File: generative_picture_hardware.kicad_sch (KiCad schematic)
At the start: 46 parts, among them J1 e_Paper_HAT, J2 Conn_ARM_JTAG_SWD_10, J3 USB_C_Receptacle_USB2.0, Q1 PMN48XP, Q2 MBT3904DW1, SW1 SW_Push, SW2 SW_Push, U1 AP2112K-3.3, U2 ESP32-WROOM-32, U3 MCP73831-2ACI-OT, U4 FT231XS, U5 SRV05-4HTG-D

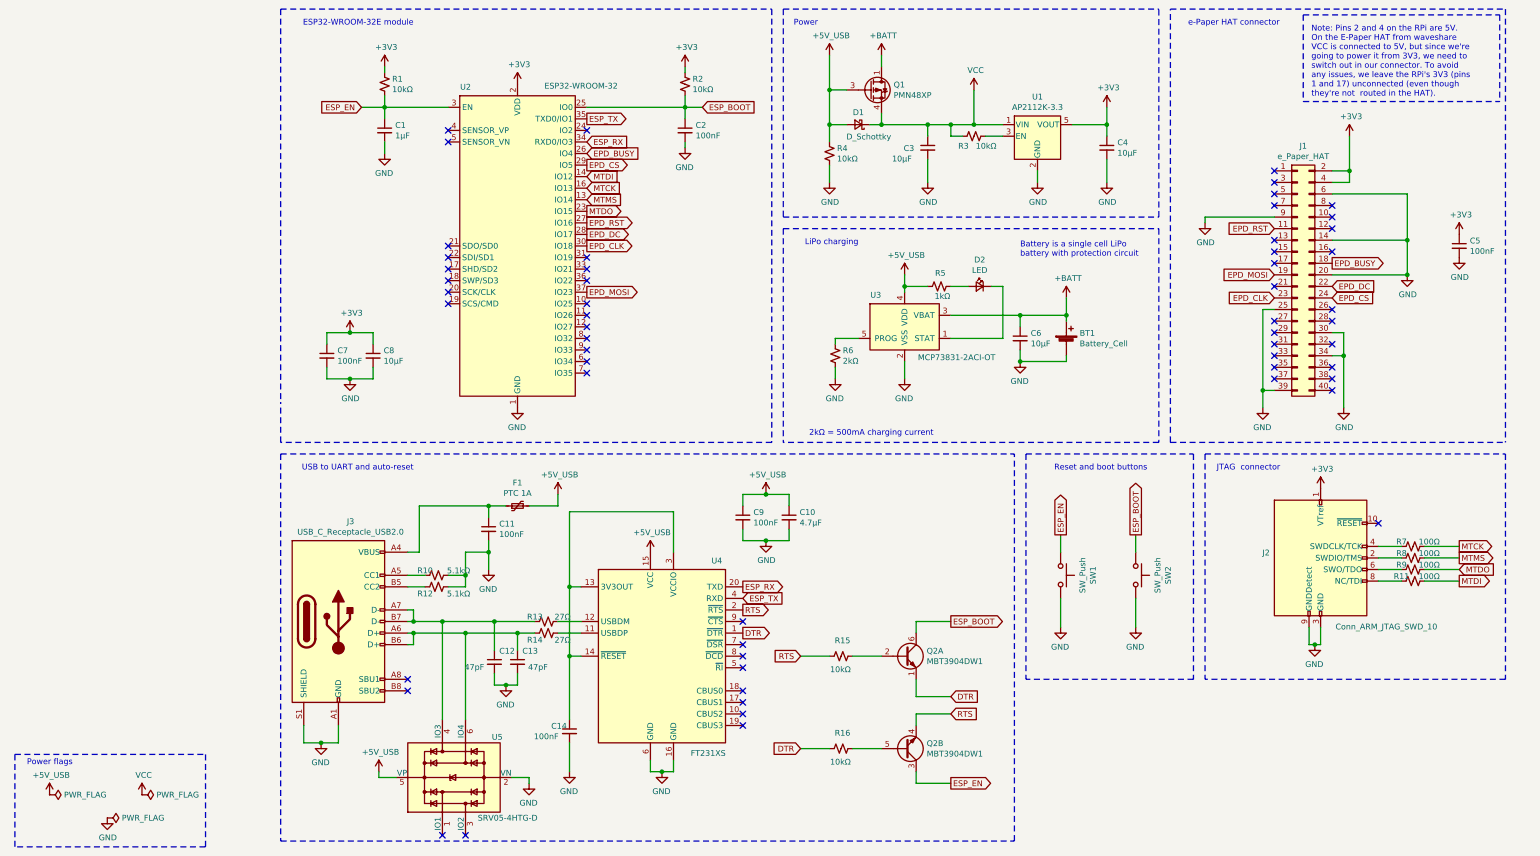
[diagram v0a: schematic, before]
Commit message: Adds battery protection circuit with AP9101
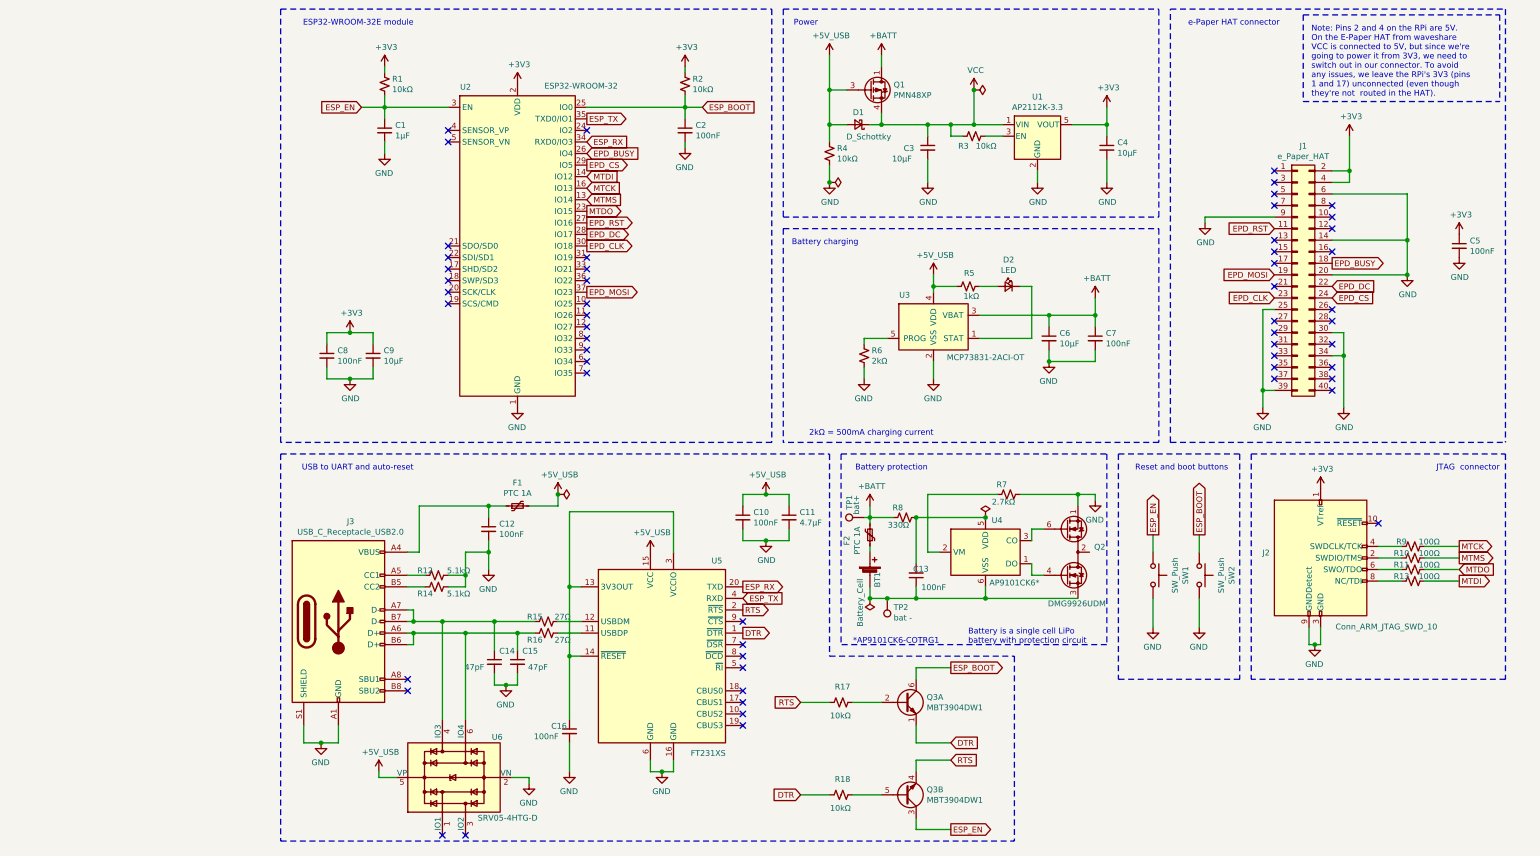
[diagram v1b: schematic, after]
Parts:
- added C13, C7: 100nF, symbol Device:C_Small
- added F2: PTC 1A, symbol Device:Polyfuse_Small
- added Q2: DMG9926UDM, Package_TO_SOT_SMD:SOT-23-6, symbol Transistor_FET:DMG9926UDM
- added R7: 2.7kΩ, symbol Device:R_Small_US
- added R8: 330Ω, symbol Device:R_Small_US
- added TP1: bat+, symbol Connector:TestPoint
- added TP2: bat -, symbol Connector:TestPoint
- added U4: AP9101CK6*, Package_TO_SOT_SMD:SOT-23-6, symbol Battery_Management:AP9101CK6
- renumbered C9 to C10, C10 to C11, C11 to C12, C12 to C14, C13 to C15, C14 to C16, C7 to C8, C8 to C9, Q2 to Q3, R8 to R10, R9 to R11, R10 to R12, R11 to R13, R12 to R14, R13 to R15, R14 to R16, R15 to R17, R16 to R18, R7 to R9, U4 to U5, U5 to U6
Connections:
- net +BATT: now also C7.1, F2.2, R8.2, TP1.1; no longer BT1.1 (+)
- net GND: now also C7.2, Q2.1 (D1), R7.1; no longer BT1.2 (-)
- new net: BT1.2 (-), C13.1, Q2.3 (S2), TP2.1, U4.6 (VSS)
- new net: BT1.1 (+), F2.1
- new net: C13.2, R8.1, U4.5 (VDD)
- new net: Q2.2 (S1/D2), Q2.5 (S1/D2)
- new net: Q2.4 (G2), U4.1 (DO)
- new net: Q2.6 (G1), U4.3 (CO)
- new net: R7.2, U4.2 (VM)
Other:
- note added: "*AP9101CK6-COTRG1"
- note added: "Battery charging"
- note added: "Battery protection"
- note removed: "LiPo charging"
- note removed: "Power flags"
- moved on the sheet: C6, D2, Q3A, Q3B, R17, R18, R5, R6, SW1, SW2, U3

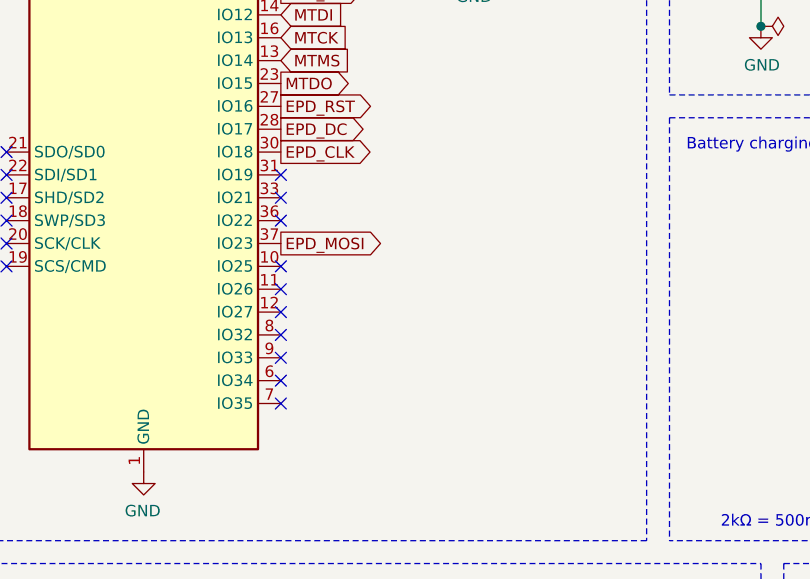
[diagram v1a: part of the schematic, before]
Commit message: Adds test points to some of the remaining GPIO pins of the ESP32
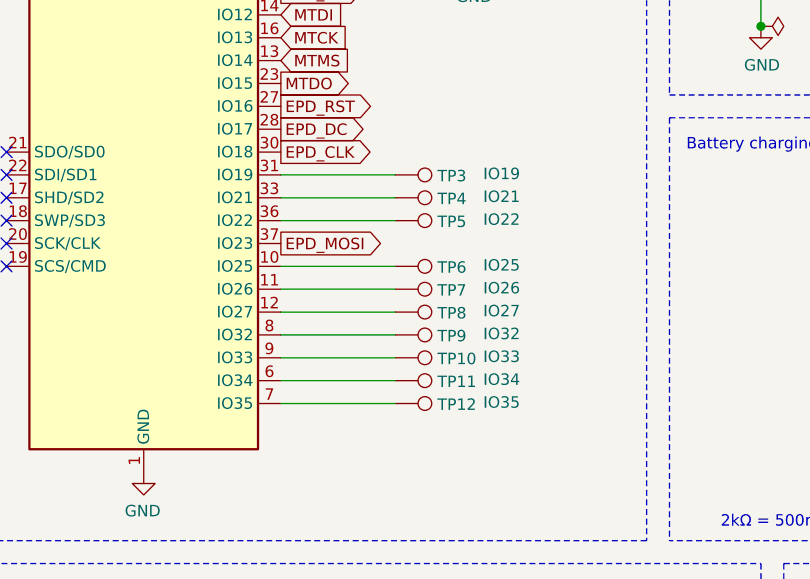
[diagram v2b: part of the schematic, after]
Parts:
- added TP10: IO33, symbol Connector:TestPoint
- added TP11: IO34, symbol Connector:TestPoint
- added TP12: IO35, symbol Connector:TestPoint
- added TP3: IO19, symbol Connector:TestPoint
- added TP4: IO21, symbol Connector:TestPoint
- added TP5: IO22, symbol Connector:TestPoint
- added TP6: IO25, symbol Connector:TestPoint
- added TP7: IO26, symbol Connector:TestPoint
- added TP8: IO27, symbol Connector:TestPoint
- added TP9: IO32, symbol Connector:TestPoint
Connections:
- net at U2.10 (IO25): now also TP6.1
- net at U2.11 (IO26): now also TP7.1
- net at U2.12 (IO27): now also TP8.1
- net at U2.31 (IO19): now also TP3.1
- net at U2.33 (IO21): now also TP4.1
- net at U2.36 (IO22): now also TP5.1
- net at U2.6 (IO34): now also TP11.1
- net at U2.7 (IO35): now also TP12.1
- net at U2.8 (IO32): now also TP9.1
- net at U2.9 (IO33): now also TP10.1
- no-connect marks 56 -> 46
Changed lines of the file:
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@@
   (no_connect (at 54.61 195.58))
   (no_connect (at 81.28 40.64))
-  (no_connect (at 81.28 68.58))
-  (no_connect (at 81.28 71.12))
-  (no_connect (at 81.28 73.66))
-  (no_connect (at 81.28 78.74))
-  (no_connect (at 81.28 81.28))
-  (no_connect (at 81.28 83.82))
-  (no_connect (at 81.28 86.36))
-  (no_connect (at 81.28 88.9))
-  (no_connect (at 81.28 91.44))
-  (no_connect (at 81.28 93.98))
   (no_connect (at 115.57 148.59))
   (no_connect (at 115.57 153.67))
@@
     (stroke (width 0) (type solid) (color 0 0 0 0))
   )
+  (wire (pts (xy 81.28 68.58) (xy 93.98 68.58))
+    (stroke (width 0) (type solid) (color 0 0 0 0))
+  )
+  (wire (pts (xy 81.28 71.12) (xy 93.98 71.12))
+    (stroke (width 0) (type solid) (color 0 0 0 0))
+  )
+  (wire (pts (xy 81.28 73.66) (xy 93.98 73.66))
+    (stroke (width 0) (type solid) (color 0 0 0 0))
+  )
+  (wire (pts (xy 81.28 78.74) (xy 93.98 78.74))
+    (stroke (width 0) (type solid) (color 0 0 0 0))
+  )
+  (wire (pts (xy 81.28 81.28) (xy 93.98 81.28))
+    (stroke (width 0) (type solid) (color 0 0 0 0))
+  )
+  (wire (pts (xy 81.28 83.82) (xy 93.98 83.82))
+    (stroke (width 0) (type solid) (color 0 0 0 0))
+  )
+  (wire (pts (xy 81.28 86.36) (xy 93.98 86.36))
+    (stroke (width 0) (type solid) (color 0 0 0 0))
+  )
+  (wire (pts (xy 81.28 88.9) (xy 93.98 88.9))
+    (stroke (width 0) (type solid) (color 0 0 0 0))
+  )
+  (wire (pts (xy 81.28 91.44) (xy 93.98 91.44))
+    (stroke (width 0) (type solid) (color 0 0 0 0))
+  )
+  (wire (pts (xy 81.28 93.98) (xy 93.98 93.98))
+    (stroke (width 0) (type solid) (color 0 0 0 0))
+  )
   (wire (pts (xy 95.25 179.07) (xy 95.25 181.61))
     (stroke (width 0) (type solid) (color 0 0 0 0))
@@
     )
     (property "Datasheet" "~" (id 3) (at 168.91 125.73 0)
+      (effects (font (size 1.27 1.27)) hide)
+    )
+  )
+  (symbol (lib_id "Connector:TestPoint") (at 93.98 68.58 270) (unit 1)
+    (in_bom yes) (on_board yes)
+    (property "Reference" "TP3" (id 0) (at 98.6791 68.7006 90)
+      (effects (font (size 1.27 1.27)) (justify left))
+    )
+    (property "Value" "IO19" (id 1) (at 103.759 68.459 90)
+      (effects (font (size 1.27 1.27)) (justify left))
+    )
+    (property "Footprint" "" (id 2) (at 93.98 73.66 0)
+      (effects (font (size 1.27 1.27)) hide)
+    )
+    (property "Datasheet" "~" (id 3) (at 93.98 73.66 0)
+      (effects (font (size 1.27 1.27)) hide)
+    )
+  )
+  (symbol (lib_id "Connector:TestPoint") (at 93.98 71.12 270) (unit 1)
+    (in_bom yes) (on_board yes)
+    (property "Reference" "TP4" (id 0) (at 98.6791 71.2406 90)
+      (effects (font (size 1.27 1.27)) (justify left))
+    )
+    (property "Value" "IO21" (id 1) (at 103.759 70.999 90)
+      (effects (font (size 1.27 1.27)) (justify left))
+    )
+    (property "Footprint" "" (id 2) (at 93.98 76.2 0)
+      (effects (font (size 1.27 1.27)) hide)
+    )
+    (property "Datasheet" "~" (id 3) (at 93.98 76.2 0)
+      (effects (font (size 1.27 1.27)) hide)
+    )
+  )
+  (symbol (lib_id "Connector:TestPoint") (at 93.98 73.66 270) (unit 1)
+    (in_bom yes) (on_board yes)
+    (property "Reference" "TP5" (id 0) (at 98.6791 73.7806 90)
+      (effects (font (size 1.27 1.27)) (justify left))
+    )
+    (property "Value" "IO22" (id 1) (at 103.759 73.539 90)
+      (effects (font (size 1.27 1.27)) (justify left))
+    )
+    (property "Footprint" "" (id 2) (at 93.98 78.74 0)
+      (effects (font (size 1.27 1.27)) hide)
+    )
+    (property "Datasheet" "~" (id 3) (at 93.98 78.74 0)
+      (effects (font (size 1.27 1.27)) hide)
+    )
+  )
+  (symbol (lib_id "Connector:TestPoint") (at 93.98 78.74 270) (unit 1)
+    (in_bom yes) (on_board yes)
+    (property "Reference" "TP6" (id 0) (at 98.6791 78.8606 90)
+      (effects (font (size 1.27 1.27)) (justify left))
+    )
+    (property "Value" "IO25" (id 1) (at 103.759 78.619 90)
+      (effects (font (size 1.27 1.27)) (justify left))
+    )
+    (property "Footprint" "" (id 2) (at 93.98 83.82 0)
+      (effects (font (size 1.27 1.27)) hide)
+    )
+    (property "Datasheet" "~" (id 3) (at 93.98 83.82 0)
+      (effects (font (size 1.27 1.27)) hide)
+    )
+  )
+  (symbol (lib_id "Connector:TestPoint") (at 93.98 81.28 270) (unit 1)
+    (in_bom yes) (on_board yes)
+    (property "Reference" "TP7" (id 0) (at 98.6791 81.4006 90)
+      (effects (font (size 1.27 1.27)) (justify left))
+    )
+    (property "Value" "IO26" (id 1) (at 103.759 81.159 90)
+      (effects (font (size 1.27 1.27)) (justify left))
+    )
+    (property "Footprint" "" (id 2) (at 93.98 86.36 0)
+      (effects (font (size 1.27 1.27)) hide)
+    )
+    (property "Datasheet" "~" (id 3) (at 93.98 86.36 0)
+      (effects (font (size 1.27 1.27)) hide)
+    )
+  )
+  (symbol (lib_id "Connector:TestPoint") (at 93.98 83.82 270) (unit 1)
+    (in_bom yes) (on_board yes)
+    (property "Reference" "TP8" (id 0) (at 98.6791 83.9406 90)
+      (effects (font (size 1.27 1.27)) (justify left))
+    )
+    (property "Value" "IO27" (id 1) (at 103.759 83.699 90)
+      (effects (font (size 1.27 1.27)) (justify left))
+    )
+    (property "Footprint" "" (id 2) (at 93.98 88.9 0)
+      (effects (font (size 1.27 1.27)) hide)
+    )
+    (property "Datasheet" "~" (id 3) (at 93.98 88.9 0)
+      (effects (font (size 1.27 1.27)) hide)
+    )
+  )
+  (symbol (lib_id "Connector:TestPoint") (at 93.98 86.36 270) (unit 1)
+    (in_bom yes) (on_board yes)
+    (property "Reference" "TP9" (id 0) (at 98.6791 86.4806 90)
+      (effects (font (size 1.27 1.27)) (justify left))
+    )
+    (property "Value" "IO32" (id 1) (at 103.759 86.239 90)
+      (effects (font (size 1.27 1.27)) (justify left))
+    )
+    (property "Footprint" "" (id 2) (at 93.98 91.44 0)
+      (effects (font (size 1.27 1.27)) hide)
+    )
+    (property "Datasheet" "~" (id 3) (at 93.98 91.44 0)
+      (effects (font (size 1.27 1.27)) hide)
+    )
+  )
+  (symbol (lib_id "Connector:TestPoint") (at 93.98 88.9 270) (unit 1)
+    (in_bom yes) (on_board yes)
+    (property "Reference" "TP10" (id 0) (at 98.6791 89.0206 90)
+      (effects (font (size 1.27 1.27)) (justify left))
+    )
+    (property "Value" "IO33" (id 1) (at 103.759 88.779 90)
+      (effects (font (size 1.27 1.27)) (justify left))
+    )
+    (property "Footprint" "" (id 2) (at 93.98 93.98 0)
+      (effects (font (size 1.27 1.27)) hide)
+    )
+    (property "Datasheet" "~" (id 3) (at 93.98 93.98 0)
+      (effects (font (size 1.27 1.27)) hide)
+    )
+  )
+  (symbol (lib_id "Connector:TestPoint") (at 93.98 91.44 270) (unit 1)
+    (in_bom yes) (on_board yes)
+    (property "Reference" "TP11" (id 0) (at 98.6791 91.5606 90)
+      (effects (font (size 1.27 1.27)) (justify left))
+    )
+    (property "Value" "IO34" (id 1) (at 103.759 91.319 90)
+      (effects (font (size 1.27 1.27)) (justify left))
+    )
+    (property "Footprint" "" (id 2) (at 93.98 96.52 0)
+      (effects (font (size 1.27 1.27)) hide)
+    )
+    (property "Datasheet" "~" (id 3) (at 93.98 96.52 0)
+      (effects (font (size 1.27 1.27)) hide)
+    )
+  )
+  (symbol (lib_id "Connector:TestPoint") (at 93.98 93.98 270) (unit 1)
+    (in_bom yes) (on_board yes)
+    (property "Reference" "TP12" (id 0) (at 98.6791 94.1006 90)
+      (effects (font (size 1.27 1.27)) (justify left))
+    )
+    (property "Value" "IO35" (id 1) (at 103.759 93.859 90)
+      (effects (font (size 1.27 1.27)) (justify left))
+    )
+    (property "Footprint" "" (id 2) (at 93.98 99.06 0)
+      (effects (font (size 1.27 1.27)) hide)
+    )
+    (property "Datasheet" "~" (id 3) (at 93.98 99.06 0)
       (effects (font (size 1.27 1.27)) hide)
     )
@@
       (reference "TP2") (unit 1) (value "bat -") (footprint "")
     )
+    (path "/d72e2e00-166f-46a4-b676-a9596746b0bd"
+      (reference "TP3") (unit 1) (value "IO19") (footprint "")
+    )
+    (path "/93e407d8-f449-49f3-bc49-49b1d072a848"
+      (reference "TP4") (unit 1) (value "IO21") (footprint "")
+    )
+    (path "/7b8a980e-33b6-435b-af52-b95a34ba2a1f"
+      (reference "TP5") (unit 1) (value "IO22") (footprint "")
+    )
+    (path "/270f2b79-8713-40da-ba21-2980f9dd1244"
+      (reference "TP6") (unit 1) (value "IO25") (footprint "")
+    )
+    (path "/b589defe-7f00-478b-8233-846d54097430"
+      (reference "TP7") (unit 1) (value "IO26") (footprint "")
+    )
+    (path "/ff9e7c25-fd02-469f-bd50-a6868ff4c8b1"
+      (reference "TP8") (unit 1) (value "IO27") (footprint "")
+    )
+    (path "/5a2c1981-279a-493b-a0f3-5e603595d1d6"
+      (reference "TP9") (unit 1) (value "IO32") (footprint "")
+    )
+    (path "/0818096d-4d51-41ad-897f-def87ec52b11"
+      (reference "TP10") (unit 1) (value "IO33") (footprint "")
+    )
+    (path "/84505109-b578-4492-a990-6aa51e85d959"
+      (reference "TP11") (unit 1) (value "IO34") (footprint "")
+    )
+    (path "/a70377e0-bdab-45c4-8047-36229c87f09f"
+      (reference "TP12") (unit 1) (value "IO35") (footprint "")
+    )
     (path "/718b170d-b1ce-42f5-b372-474f1687d990"

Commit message: Adds a second LED to indicate the charging is complete and assigns some footprints
As per table 5-1 in the MCP73831 datasheet[1], the STAT pin is low while
charging, high when charge is complete and high impedance when the IC is
shutdown or there is no battery present:

+----------+--------+
| Charging |STAT pin|
+----------+--------+
| shutdown | High Z |
| No batt  | High Z |
| Precond. |    L   |
| Const. I |    L   |
| Const. V |    L   |
| Complete |    H   |
+----------+--------+

This second LED could just not be populated if just turning off the LED
is the prefered way to signal that charging is done.

[1]: http://ww1.microchip.com/downloads/en/DeviceDoc/20001984g.pdf
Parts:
- added D3: green, symbol Device:LED_Small
- added R19: 1kΩ, symbol Device:R_Small_US
- BT1: footprint (none) -> Connector_JST:JST_PH_S2B-PH-SM4-TB_1x02-1MP_P2.00mm_Horizontal
- C1, C10, C11, C12, C13, C14, C15, C16, C2, C3, C4, C5, C6, C7, C8, C9: footprint (none) -> Capacitor_SMD:C_0805_2012Metric_Pad1.18x1.45mm_HandSolder
- D2: value LED -> yellow
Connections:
- net GND: now also D3.1 (K)
- net at D2.1 (K), U3.1 (STAT): now also R19.1
- new net: D3.2 (A), R19.2

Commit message: Associates footprints to components in the schematics
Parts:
- D1: value D_Schottky -> MBR120; footprint (none) -> Diode_SMD:D_SOD-123
- D2, D3: footprint (none) -> LED_SMD:LED_0805_2012Metric_Pad1.15x1.40mm_HandSolder
- F1, F2: footprint (none) -> Generative_picture:Fuse_Bourns_MF-NSHT
- J1: footprint (none) -> Connector_PinHeader_2.54mm:PinHeader_2x20_P2.54mm_Vertical
- J2: footprint (none) -> Connector_PinHeader_2.54mm:PinHeader_2x05_P2.54mm_Vertical
- J3: footprint (none) -> Generative_picture:USB_C_Receptacle_JAE_DX07S016JA1
- R1, R10, R11, R12, R13, R14, R15, R16, R17, R18, R19, R2, R3, R4, R5, R6, R7, R8, R9: footprint (none) -> Resistor_SMD:R_0805_2012Metric_Pad1.20x1.40mm_HandSolder
- SW1, SW2: footprint (none) -> Generative_picture:SWITCH_TACTILE_CK_PTS636_SK43_SMTR_LFS
- TP1, TP10, TP11, TP12, TP2, TP3, TP4, TP5, TP6, TP7, TP8, TP9: footprint (none) -> TestPoint:TestPoint_Pad_D2.0mm
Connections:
- net ESP_EN: now also Q3.4 (E2); no longer Q3.3 (C2)
- net RTS: now also Q3.3 (C2); no longer Q3.4 (E2)

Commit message: Assigns custom footprint for e-Paper display HAT
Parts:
- J1: footprint Connector_PinHeader_2.54mm:PinHeader_2x20_P2.54mm_Vertical -> Generative_picture:e-Paper_display_HAT
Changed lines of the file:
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@@
     (property "Reference" "J1" (id 0) (at 238.76 44.0498 0))
     (property "Value" "e_Paper_HAT" (id 1) (at 238.76 46.349 0))
-    (property "Footprint" "Connector_PinHeader_2.54mm:PinHeader_2x20_P2.54mm_Vertical" (id 2) (at 237.49 72.39 0)
+    (property "Footprint" "Generative_picture:e-Paper_display_HAT" (id 2) (at 237.49 72.39 0)
       (effects (font (size 1.27 1.27)) hide)
     )
@@
     )
     (path "/709e9e91-e8c6-418a-9347-6219920aa396"
-      (reference "J1") (unit 1) (value "e_Paper_HAT") (footprint "Connector_PinHeader_2.54mm:PinHeader_2x20_P2.54mm_Vertical")
+      (reference "J1") (unit 1) (value "e_Paper_HAT") (footprint "Generative_picture:e-Paper_display_HAT")
     )
     (path "/0213688c-2bf6-4865-b282-51d39e8a357d"

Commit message: Renames e-Paper DIN pin
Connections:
- net EPD_MOSI renamed EPD_DIN
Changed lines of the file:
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@@
     )
   )
-  (global_label "EPD_MOSI" (shape output) (at 81.28 76.2 0)
+  (global_label "EPD_DIN" (shape output) (at 81.28 76.2 0)
     (effects (font (size 1.27 1.27)) (justify left))
-    (property "Intersheet References" "${INTERSHEET_REFS}" (id 0) (at 94.47 76.1206 0)
+    (property "Intersheet References" "${INTERSHEET_REFS}" (id 0) (at 93.079 76.1206 0)
       (effects (font (size 1.27 1.27)) (justify left) hide)
     )
@@
     )
   )
-  (global_label "EPD_MOSI" (shape input) (at 232.41 72.39 180)
+  (global_label "EPD_DIN" (shape input) (at 232.41 72.39 180)
     (effects (font (size 1.27 1.27)) (justify right))
-    (property "Intersheet References" "${INTERSHEET_REFS}" (id 0) (at 219.22 72.3106 0)
+    (property "Intersheet References" "${INTERSHEET_REFS}" (id 0) (at 220.611 72.3106 0)
       (effects (font (size 1.27 1.27)) (justify right) hide)
     )
